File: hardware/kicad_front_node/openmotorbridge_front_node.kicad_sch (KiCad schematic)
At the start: 0 parts

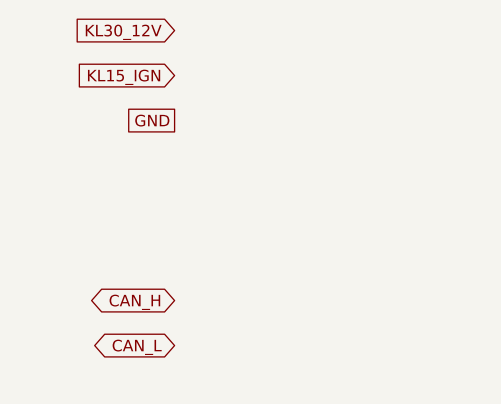
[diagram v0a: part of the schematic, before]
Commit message: feat(hardware): upgrade front node power architecture to dual power (pure USB bus-powered default + optional switched 12V KL15)
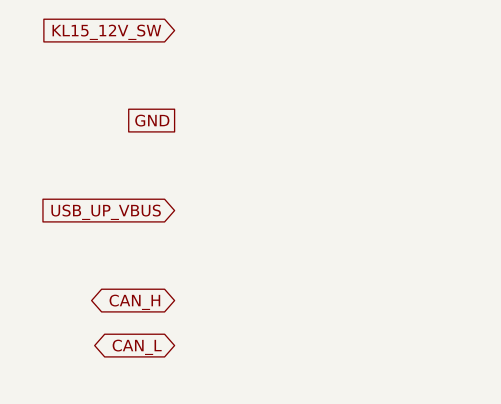
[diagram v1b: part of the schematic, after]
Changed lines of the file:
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@@
 		(title "OpenMotorBridge Universal Front Node (Cockpit & Smart Fairing)")
 		(date "2026-09-03")
-		(rev "v1.0")
+		(rev "v1.1")
 		(company "OpenMotorBridge Open Source Hardware")
-		(comment 1 "Automotive USB 2.0 Hub + CarPlay Power Switch + I2S Ambient Mic + CAN + Handlebar PTT + ESP-NOW")
+		(comment 1 "Dual Power: Pure USB Bus-Powered Standard + Optional Switched 12V (KL15 ACC)")
 	)
-	(global_label "KL30_12V" (shape input) (at 30.0 40.0 180) (effects (font (size 1.27 1.27)) (justify right)))
-	(global_label "KL15_IGN" (shape input) (at 30.0 45.0 180) (effects (font (size 1.27 1.27)) (justify right)))
+	(global_label "KL15_12V_SW" (shape input) (at 30.0 40.0 180) (effects (font (size 1.27 1.27)) (justify right)))
 	(global_label "GND" (shape passive) (at 30.0 50.0 180) (effects (font (size 1.27 1.27)) (justify right)))
+	(global_label "USB_UP_VBUS" (shape input) (at 30.0 60.0 180) (effects (font (size 1.27 1.27)) (justify right)))
 	(global_label "VCC_5V" (shape output) (at 80.0 40.0 0) (effects (font (size 1.27 1.27)) (justify left)))
 	(global_label "VCC_3V3" (shape output) (at 80.0 45.0 0) (effects (font (size 1.27 1.27)) (justify left)))

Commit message: docs & feat: restructure Chapter 08 reference kits, update modular enclosures, front-node mechanics and firmware
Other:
- title: OpenMotorBridge Universal Front Node (Cockpit & Smart Fairing) -> OpenMotorBridge Universal Front Node (Cockpit & Sensor Hub)
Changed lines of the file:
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@@
 	(paper "A3")
 	(title_block
-		(title "OpenMotorBridge Universal Front Node (Cockpit & Smart Fairing)")
+		(title "OpenMotorBridge Universal Front Node (Cockpit & Sensor Hub)")
 		(date "2026-09-03")
 		(rev "v1.1")

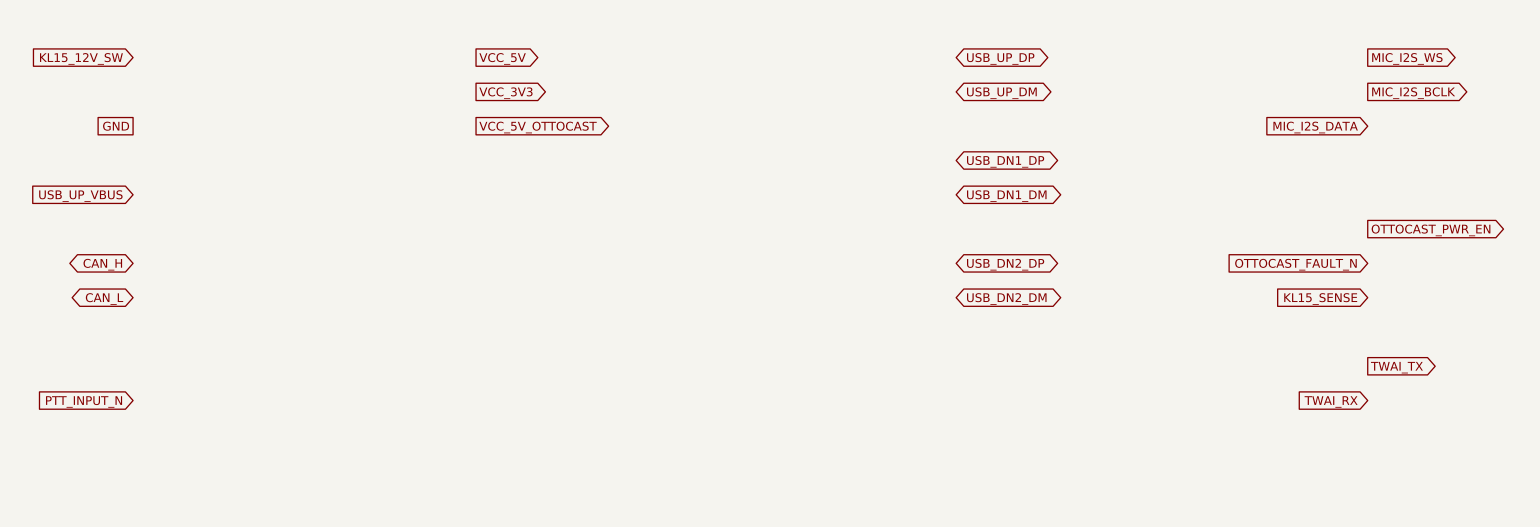
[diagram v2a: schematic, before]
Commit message: feat(hw,fw,pwa): implement PCBA 05 Front Node, LoRa alarm pager, universal TPMS, ESS strobe, privacy mute, and video telemetry export
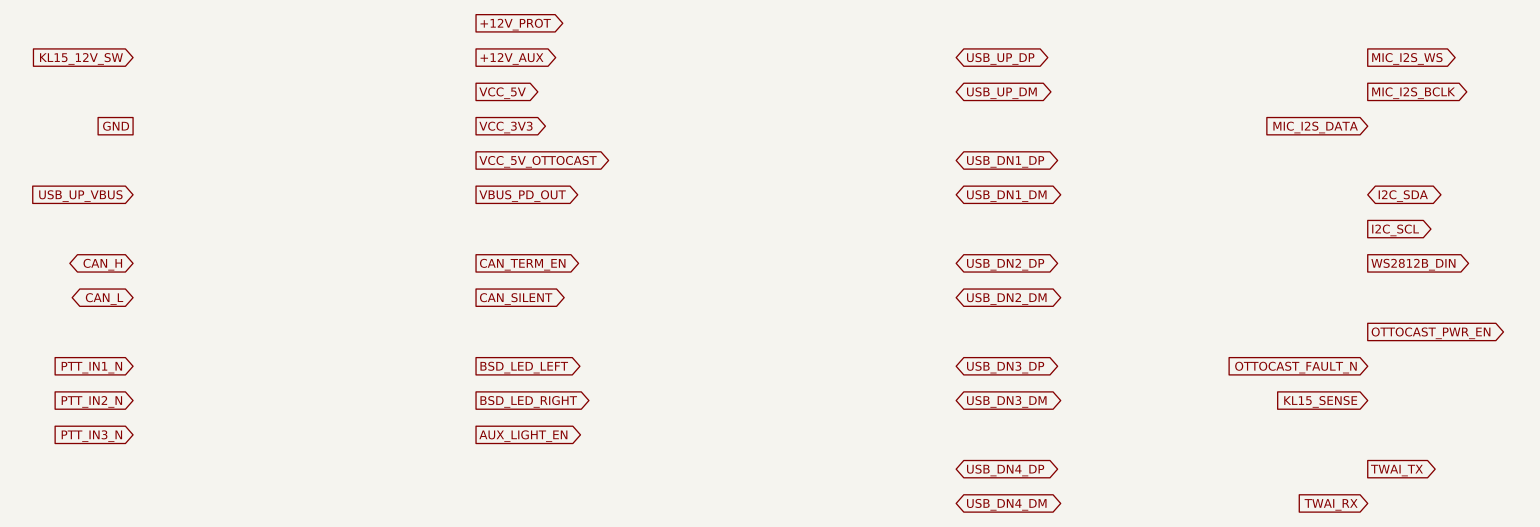
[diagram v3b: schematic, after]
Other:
- title: OpenMotorBridge Universal Front Node (Cockpit & Sensor Hub) -> OpenMotorBridge Universal Front Node (Cockpit & Sensor Hub PCBA 05)
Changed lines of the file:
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@@
 	(paper "A3")
 	(title_block
-		(title "OpenMotorBridge Universal Front Node (Cockpit & Sensor Hub)")
-		(date "2026-09-03")
-		(rev "v1.1")
+		(title "OpenMotorBridge Universal Front Node (Cockpit & Sensor Hub PCBA 05)")
+		(date "2026-09-12")
+		(rev "v2.0")
 		(company "OpenMotorBridge Open Source Hardware")
-		(comment 1 "Dual Power: Pure USB Bus-Powered Standard + Optional Switched 12V (KL15 ACC)")
+		(comment 1 "ESP32-S3, USB2514B 4-Port Hub, SC8102 USB-PD 20W, Qi 12V, Aux Light, BSD LEDs")
 	)
 	(global_label "KL15_12V_SW" (shape input) (at 30.0 40.0 180) (effects (font (size 1.27 1.27)) (justify right)))
+	(global_label "+12V_PROT" (shape output) (at 80.0 35.0 0) (effects (font (size 1.27 1.27)) (justify left)))
+	(global_label "+12V_AUX" (shape output) (at 80.0 40.0 0) (effects (font (size 1.27 1.27)) (justify left)))
 	(global_label "GND" (shape passive) (at 30.0 50.0 180) (effects (font (size 1.27 1.27)) (justify right)))
 	(global_label "USB_UP_VBUS" (shape input) (at 30.0 60.0 180) (effects (font (size 1.27 1.27)) (justify right)))
-	(global_label "VCC_5V" (shape output) (at 80.0 40.0 0) (effects (font (size 1.27 1.27)) (justify left)))
-	(global_label "VCC_3V3" (shape output) (at 80.0 45.0 0) (effects (font (size 1.27 1.27)) (justify left)))
-	(global_label "VCC_5V_OTTOCAST" (shape output) (at 80.0 50.0 0) (effects (font (size 1.27 1.27)) (justify left)))
+	(global_label "VCC_5V" (shape output) (at 80.0 45.0 0) (effects (font (size 1.27 1.27)) (justify left)))
+	(global_label "VCC_3V3" (shape output) (at 80.0 50.0 0) (effects (font (size 1.27 1.27)) (justify left)))
+	(global_label "VCC_5V_OTTOCAST" (shape output) (at 80.0 55.0 0) (effects (font (size 1.27 1.27)) (justify left)))
+	(global_label "VBUS_PD_OUT" (shape output) (at 80.0 60.0 0) (effects (font (size 1.27 1.27)) (justify left)))
 	(global_label "CAN_H" (shape bidirectional) (at 30.0 70.0 180) (effects (font (size 1.27 1.27)) (justify right)))
 	(global_label "CAN_L" (shape bidirectional) (at 30.0 75.0 180) (effects (font (size 1.27 1.27)) (justify right)))
-	(global_label "PTT_INPUT_N" (shape input) (at 30.0 90.0 180) (effects (font (size 1.27 1.27)) (justify right)))
+	(global_label "CAN_TERM_EN" (shape output) (at 80.0 70.0 0) (effects (font (size 1.27 1.27)) (justify left)))
+	(global_label "CAN_SILENT" (shape output) (at 80.0 75.0 0) (effects (font (size 1.27 1.27)) (justify left)))
+	(global_label "PTT_IN1_N" (shape input) (at 30.0 85.0 180) (effects (font (size 1.27 1.27)) (justify right)))
+	(global_label "PTT_IN2_N" (shape input) (at 30.0 90.0 180) (effects (font (size 1.27 1.27)) (justify right)))
+	(global_label "PTT_IN3_N" (shape input) (at 30.0 95.0 180) (effects (font (size 1.27 1.27)) (justify right)))
+	(global_label "BSD_LED_LEFT" (shape output) (at 80.0 85.0 0) (effects (font (size 1.27 1.27)) (justify left)))
+	(global_label "BSD_LED_RIGHT" (shape output) (at 80.0 90.0 0) (effects (font (size 1.27 1.27)) (justify left)))
+	(global_label "AUX_LIGHT_EN" (shape output) (at 80.0 95.0 0) (effects (font (size 1.27 1.27)) (justify left)))
 	(global_label "USB_UP_DP" (shape bidirectional) (at 150.0 40.0 0) (effects (font (size 1.27 1.27)) (justify left)))
 	(global_label "USB_UP_DM" (shape bidirectional) (at 150.0 45.0 0) (effects (font (size 1.27 1.27)) (justify left)))
@@
 	(global_label "USB_DN2_DP" (shape bidirectional) (at 150.0 70.0 0) (effects (font (size 1.27 1.27)) (justify left)))
 	(global_label "USB_DN2_DM" (shape bidirectional) (at 150.0 75.0 0) (effects (font (size 1.27 1.27)) (justify left)))
+	(global_label "USB_DN3_DP" (shape bidirectional) (at 150.0 85.0 0) (effects (font (size 1.27 1.27)) (justify left)))
+	(global_label "USB_DN3_DM" (shape bidirectional) (at 150.0 90.0 0) (effects (font (size 1.27 1.27)) (justify left)))
+	(global_label "USB_DN4_DP" (shape bidirectional) (at 150.0 100.0 0) (effects (font (size 1.27 1.27)) (justify left)))
+	(global_label "USB_DN4_DM" (shape bidirectional) (at 150.0 105.0 0) (effects (font (size 1.27 1.27)) (justify left)))
 	(global_label "MIC_I2S_WS" (shape output) (at 210.0 40.0 0) (effects (font (size 1.27 1.27)) (justify left)))
 	(global_label "MIC_I2S_BCLK" (shape output) (at 210.0 45.0 0) (effects (font (size 1.27 1.27)) (justify left)))
 	(global_label "MIC_I2S_DATA" (shape input) (at 210.0 50.0 180) (effects (font (size 1.27 1.27)) (justify right)))
-	(global_label "OTTOCAST_PWR_EN" (shape output) (at 210.0 65.0 0) (effects (font (size 1.27 1.27)) (justify left)))
-	(global_label "OTTOCAST_FAULT_N" (shape input) (at 210.0 70.0 180) (effects (font (size 1.27 1.27)) (justify right)))
-	(global_label "KL15_SENSE" (shape input) (at 210.0 75.0 180) (effects (font (size 1.27 1.27)) (justify right)))
-	(global_label "TWAI_TX" (shape output) (at 210.0 85.0 0) (effects (font (size 1.27 1.27)) (justify left)))
-	(global_label "TWAI_RX" (shape input) (at 210.0 90.0 180) (effects (font (size 1.27 1.27)) (justify right)))
+	(global_label "I2C_SDA" (shape bidirectional) (at 210.0 60.0 0) (effects (font (size 1.27 1.27)) (justify left)))
+	(global_label "I2C_SCL" (shape output) (at 210.0 65.0 0) (effects (font (size 1.27 1.27)) (justify left)))
+	(global_label "WS2812B_DIN" (shape output) (at 210.0 70.0 0) (effects (font (size 1.27 1.27)) (justify left)))
+	(global_label "OTTOCAST_PWR_EN" (shape output) (at 210.0 80.0 0) (effects (font (size 1.27 1.27)) (justify left)))
+	(global_label "OTTOCAST_FAULT_N" (shape input) (at 210.0 85.0 180) (effects (font (size 1.27 1.27)) (justify right)))
+	(global_label "KL15_SENSE" (shape input) (at 210.0 90.0 180) (effects (font (size 1.27 1.27)) (justify right)))
+	(global_label "TWAI_TX" (shape output) (at 210.0 100.0 0) (effects (font (size 1.27 1.27)) (justify left)))
+	(global_label "TWAI_RX" (shape input) (at 210.0 105.0 180) (effects (font (size 1.27 1.27)) (justify right)))
 )

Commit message: feat(hardware): implement dual independent 20W USB-PD subsystem for Lenker and Handschuhfach on PCBA 05
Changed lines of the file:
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@@
 	(title_block
 		(title "OpenMotorBridge Universal Front Node (Cockpit & Sensor Hub PCBA 05)")
-		(date "2026-09-12")
-		(rev "v2.0")
+		(date "2026-09-13")
+		(rev "v2.1")
 		(company "OpenMotorBridge Open Source Hardware")
-		(comment 1 "ESP32-S3, USB2514B 4-Port Hub, SC8102 USB-PD 20W, Qi 12V, Aux Light, BSD LEDs")
+		(comment 1 "ESP32-S3, USB2514B Hub, Dual SW3526 USB-PD 20W, Qi 12V, Aux Light, BSD LEDs")
 	)
 	(global_label "KL15_12V_SW" (shape input) (at 30.0 40.0 180) (effects (font (size 1.27 1.27)) (justify right)))
@@
 	(global_label "VCC_3V3" (shape output) (at 80.0 50.0 0) (effects (font (size 1.27 1.27)) (justify left)))
 	(global_label "VCC_5V_OTTOCAST" (shape output) (at 80.0 55.0 0) (effects (font (size 1.27 1.27)) (justify left)))
-	(global_label "VBUS_PD_OUT" (shape output) (at 80.0 60.0 0) (effects (font (size 1.27 1.27)) (justify left)))
+	(global_label "VBUS_PD1_OUT" (shape output) (at 80.0 60.0 0) (effects (font (size 1.27 1.27)) (justify left)))
+	(global_label "VBUS_PD3_OUT" (shape output) (at 80.0 65.0 0) (effects (font (size 1.27 1.27)) (justify left)))
 	(global_label "CAN_H" (shape bidirectional) (at 30.0 70.0 180) (effects (font (size 1.27 1.27)) (justify right)))
 	(global_label "CAN_L" (shape bidirectional) (at 30.0 75.0 180) (effects (font (size 1.27 1.27)) (justify right)))
@@
 	(global_label "BSD_LED_RIGHT" (shape output) (at 80.0 90.0 0) (effects (font (size 1.27 1.27)) (justify left)))
 	(global_label "AUX_LIGHT_EN" (shape output) (at 80.0 95.0 0) (effects (font (size 1.27 1.27)) (justify left)))
+	(global_label "USB_DN1_CC" (shape bidirectional) (at 80.0 100.0 0) (effects (font (size 1.27 1.27)) (justify left)))
+	(global_label "USB_DN3_CC" (shape bidirectional) (at 80.0 105.0 0) (effects (font (size 1.27 1.27)) (justify left)))
 	(global_label "USB_UP_DP" (shape bidirectional) (at 150.0 40.0 0) (effects (font (size 1.27 1.27)) (justify left)))
 	(global_label "USB_UP_DM" (shape bidirectional) (at 150.0 45.0 0) (effects (font (size 1.27 1.27)) (justify left)))

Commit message: feat(hw): finalize PCB lineup routing, sync PCBA 03 cartridge with J_PROG header and DTM12 schematics
- PCBA 01 (Central Box): Remediate net routing, DTM12 hierarchical schematic synchronization, 100% routed, 0 DRC errors.
- PCBA 03 (Smart Modular Cartridge): Position and route J_PROG 4-pin SMD programming header on F.Cu at (108.0, 89.61), synchronize CPL and schematic, 100% routed, 0 DRC errors.
- PCBA 05 (Universal Front Node): Preconnect and routing verified, 100% routed, 0 DRC errors.
- PCBA 07 (LoRa Smart-Keyfob): Routing and DRC verified, 100% routed, 0 DRC errors.
- PCBA 08 (Radar 2.0 Sub-MCU & Wings): Sub-MCU routing and HF isolation verified, 100% routed, 0 DRC errors.
- PCBA 10 (OMM 446 PMR/DMR Intercom): KiCad DRC verified, 100% routed, 0 DRC errors.
- Firmware: Align configuration headers across front_node and smart_cartridge.
- Tools: Add comprehensive preflight PCBA audit suite tools/audit_pcbas_preflight.py.
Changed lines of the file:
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@@
 	(global_label "TWAI_TX" (shape output) (at 210.0 100.0 0) (effects (font (size 1.27 1.27)) (justify left)))
 	(global_label "TWAI_RX" (shape input) (at 210.0 105.0 180) (effects (font (size 1.27 1.27)) (justify right)))
+	(global_label "UWB_SCK" (shape output) (at 210.0 115.0 0) (effects (font (size 1.27 1.27)) (justify left)))
+	(global_label "UWB_MOSI" (shape output) (at 210.0 120.0 0) (effects (font (size 1.27 1.27)) (justify left)))
+	(global_label "UWB_MISO" (shape input) (at 210.0 125.0 180) (effects (font (size 1.27 1.27)) (justify right)))
+	(global_label "UWB_CS" (shape output) (at 210.0 130.0 0) (effects (font (size 1.27 1.27)) (justify left)))
+	(global_label "UWB_IRQ" (shape input) (at 210.0 135.0 180) (effects (font (size 1.27 1.27)) (justify right)))
+	(global_label "UWB_RST" (shape output) (at 210.0 140.0 0) (effects (font (size 1.27 1.27)) (justify left)))
+	(global_label "UWB_RF" (shape passive) (at 210.0 145.0 0) (effects (font (size 1.27 1.27)) (justify left)))
 )

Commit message: fix(frontnode): synchronize PCBA 05 schematic with PCB and pass prefab-gate check
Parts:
- added ANT_UWB: Taoglas_FXUWB10, Connector_Coaxial:U.FL_Hirose_U.FL-R-SMT-1_Vertical, symbol ANT_UWB_sym
- added C19: 10uF_50V, C_0805_2012Metric, symbol C19_sym
- added C22: 22uF_16V, C_0805_2012Metric, symbol C22_sym
- added C24: 2.2uF_3V3, C_0603_1608Metric, symbol C24_sym
- added C25: 10uF_50V_PD1, C_0805_2012Metric, symbol C25_sym
- added C26: 22uF_25V_PD1, C_0805_2012Metric, symbol C26_sym
- added C27: 10uF_50V_PD3, C_0805_2012Metric, symbol C27_sym
- added C28: 22uF_25V_PD3, C_0805_2012Metric, symbol C28_sym
- added C_BUF: 470uF_10V_POLYMER, CP_EIA-7343-31_Kemet-D, symbol C_BUF_sym
- added D4: SMCJ36CA_TVS, D_SMB, symbol D4_sym
- added D5: SS34_REV_POL, D_SMA, symbol D5_sym
- added D7: SS34_USB_OR, D_SMA, symbol D7_sym
- added D8: SS34_BUCK_OR, D_SMA, symbol D8_sym
- added H1: M2.5_MOUNT, MountingHole_2.7mm_M2.5_Pad_Via, symbol H1_sym
- added H2: M2.5_MOUNT, MountingHole_2.7mm_M2.5_Pad_Via, symbol H2_sym
- added H3: M2.5_MOUNT, MountingHole_2.7mm_M2.5_Pad_Via, symbol H3_sym
- added H4: M2.5_MOUNT, MountingHole_2.7mm_M2.5_Pad_Via, symbol H4_sym
- added J1: 12V_KL15_GND, JST_PH_B2B-PH-K_1x02_P2.00mm_Vertical, symbol J1_sym
- added J10: 12V_QI_POWER, JST_PH_B2B-PH-K_1x02_P2.00mm_Vertical, symbol J10_sym
- added J11: 12V_AUX_LIGHT, JST_PH_B2B-PH-K_1x02_P2.00mm_Vertical, symbol J11_sym
- added J12: QWIIC_I2C, JST_SH_BM04B-SRSS-TB_1x04-1MP_P1.00mm_Vertical, symbol J12_sym
- added J2: CAN_H_L_GND, JST_PH_B3B-PH-K_1x03_P2.00mm_Vertical, symbol J2_sym
- added J3: HANDLEBAR_MULTI_BTN, JST_PH_B4B-PH-K_1x04_P2.00mm_Vertical, symbol J3_sym
- added J4: USB_UPSTREAM_HOST, JST_PH_B4B-PH-K_1x04_P2.00mm_Vertical, symbol J4_sym
- added J5: USB_DN1_PHONE_PD20W, JST_PH_B5B-PH-K_1x05_P2.00mm_Vertical, symbol J5_sym
- added J5_MP3: USB_DN3_GLOVEBOX_PD20W, JST_PH_B5B-PH-K_1x05_P2.00mm_Vertical, symbol J5_MP3_sym
- added J6: USB_DN2_CP2AA_PIGTAIL, JST_PH_B4B-PH-K_1x04_P2.00mm_Vertical, symbol J6_sym
- added J6_AUX: USB_DN4_COCKPIT_AUX, JST_PH_B4B-PH-K_1x04_P2.00mm_Vertical, symbol J6_AUX_sym
- added J7: USB-C_SERVICE, USB_C_Receptacle_HRO_TYPE-C-31-M-12, symbol J7_sym
- added J8: ACTION_CAM_5V_PWR, JST_PH_B2B-PH-K_1x02_P2.00mm_Vertical, symbol J8_sym
- added J9: MIRROR_BSD_LEDS, JST_PH_B3B-PH-K_1x03_P2.00mm_Vertical, symbol J9_sym
- added K1: CPC1017N_CAN_RELAY, SOP-4_4.4x2.6mm_P1.27mm, symbol K1_sym
- added L1: 4.7uH_Power_Choke, L_Sunlord_MWSA1206S-470, symbol L1_sym
- added L2: 4.7uH_PD1_Choke, L_Sunlord_MWSA0503S, symbol L2_sym
- added L3: 4.7uH_PD3_Choke, L_Sunlord_MWSA0503S, symbol L3_sym
- added LED1: WS2812B-2020_RGB, LED_WS2812B-2020_PLCC4_2.0x2.0mm, symbol LED1_sym
- added MIC1: MSM261S4030H0R, InvenSense_ICS-43434-6_3.5x2.65mm, symbol MIC1_sym
- added MK1: SPH0645LM4H, Sensor_Audio:Knowles_SPH0645LM4H, symbol MK1_sym
- added Q1: DMN63D8_BSD_MOSFET, SOT-363_SC-70-6, symbol Q1_sym
- added Q2: TPS1H100_AUX_LIGHT, Texas_HTSSOP-14-1EP_4.4x5mm_P0.65mm_EP3.4x5mm_Mask3.155x3.255mm_ThermalVias, symbol Q2_sym
- added R10: 120R_CAN, R_0603_1608Metric, symbol R10_sym
- added R15: 5.1k_CC1, R_0603_1608Metric, symbol R15_sym
- added R16: 5.1k_CC2, R_0603_1608Metric, symbol R16_sym
- added R5: 12k_RBIAS, R_0603_1608Metric, symbol R5_sym
- added R8: 10k_FAULT, R_0603_1608Metric, symbol R8_sym
- added SW1: BOOT, SW_Push_SPST_NO_Alps_SKRK, symbol SW1_sym
- added SW2: RESET, SW_Push_SPST_NO_Alps_SKRK, symbol SW2_sym
- added U1: ESP32-S3-WROOM-1U, ESP32-S3-WROOM-1U, symbol U1_sym
- added U2: USB2514Bi-AEZG, QFN-36-1EP_6x6mm_P0.5mm_EP4.1x4.1mm, symbol U2_sym
- added U3: TPS54302_5V_BUCK, SOT-23-6, symbol U3_sym
- added U4: TPS2051B_PORT2_GATE, SOT-23-5, symbol U4_sym
- added U5: SW3526_USB_PD1_20W, QFN-28-1EP_4x4mm_P0.4mm_EP2.4x2.4mm_ThermalVias, symbol U5_sym
- added U6: TCAN334G_CAN, SOIC-8_3.9x4.9mm_P1.27mm, symbol U6_sym
- added U7: TLV75533P_3V3_LDO, SOT-23-5, symbol U7_sym
- added U8: SW3526_USB_PD3_20W, QFN-28-1EP_4x4mm_P0.4mm_EP2.4x2.4mm_ThermalVias, symbol U8_sym
- added U9: DW3110, Package_DFN_QFN:QFN-16-1EP_3x3mm_P0.5mm_EP1.7x1.7mm_ThermalVias, symbol U9_sym
- added Y1: 24.000MHz, Crystal_SMD_3225-4Pin_3.2x2.5mm, symbol Y1_sym
- added Y_UWB: 38.4MHz, Crystal:Crystal_SMD_2016-4Pin_2.0x1.6mm, symbol Y_UWB_sym
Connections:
- net +12V_AUX: now also J11.1 (+12V_AUX), Q2.6 (+12V_AUX), Q2.7 (+12V_AUX), Q2.8 (+12V_AUX)
- net +12V_PROT: now also C19.1 (+12V_PROT), C25.1 (+12V_PROT), C27.1 (+12V_PROT), D4.1 (+12V_PROT), D5.2 (+12V_PROT), J10.1 (+12V_PROT), J9.1 (+12V_PROT), Q2.11 (+12V_PROT), Q2.12 (+12V_PROT), Q2.13 (+12V_PROT), Q2.14 (+12V_PROT), Q2.15 (+12V_PROT), U3.3 (+12V_PROT), U3.5 (+12V_PROT), U5.1 (+12V_PROT), U5.2 (+12V_PROT), U5.28 (+12V_PROT), U8.1 (+12V_PROT), U8.2 (+12V_PROT), U8.28 (+12V_PROT)
- net AUX_LIGHT_EN: now also Q2.2 (AUX_LIGHT_EN), U1.22 (AUX_LIGHT_EN)
- net BSD_LED_LEFT: now also Q1.2 (BSD_LED_LEFT), U1.20 (BSD_LED_LEFT)
- net BSD_LED_RIGHT: now also Q1.5 (BSD_LED_RIGHT), U1.21 (BSD_LED_RIGHT)
- net CAN_H: now also J2.1 (CAN_H), K1.3 (CAN_H), U6.7 (CAN_H)
- net CAN_L: now also J2.2 (CAN_L), R10.2 (CAN_L), U6.6 (CAN_L)
- net CAN_SILENT: now also U1.5 (CAN_SILENT), U6.8 (CAN_SILENT)
- net CAN_TERM_EN: now also K1.1 (CAN_TERM_EN), U1.15 (CAN_TERM_EN)
- net GND: now also ANT_UWB.2 (GND), C19.2 (GND), C22.2 (GND), C24.2 (GND), C25.2 (GND), C26.2 (GND), C27.2 (GND), C28.2 (GND), C_BUF.2 (GND), D4.2 (GND), H1.1 (GND), H2.1 (GND), H3.1 (GND), H4.1 (GND), J1.2 (GND), J10.2 (GND), J11.2 (GND), J12.1 (GND), J12.MP (GND), J2.3 (GND), J3.1 (GND), J4.4 (GND), J5.5 (GND), J5_MP3.5 (GND), J6.4 (GND), J6_AUX.4 (GND), J7.A1 (GND), J7.A12 (GND), J7.B1 (GND), J7.B12 (GND), J7.SH (GND), J8.2 (GND), K1.2 (GND), LED1.2 (GND), LED1.3 (GND), MIC1.2 (GND), MIC1.3 (GND), MK1.5 (GND), Q1.1 (GND), Q1.4 (GND), Q2.1 (GND), Q2.4 (GND), R15.2 (GND), R16.2 (GND), R5.2 (GND), SW1.2 (GND), SW2.2 (GND), U1.1 (GND), U1.40 (GND), U1.41 (GND), U2.11 (GND), U2.25 (GND), U2.28 (GND), U2.34 (GND), U2.37 (GND), U3.1 (GND), U4.2 (GND), U5.14 (GND), U5.29 (GND), U6.2 (GND), U6.5 (GND), U7.2 (GND), U7.4 (GND), U8.14 (GND), U8.29 (GND), U9.1 (GND), U9.11 (GND), U9.16 (GND), U9.17 (GND), U9.2 (GND), U9.3 (GND), U9.6 (GND), Y1.2 (GND), Y1.4 (GND), Y_UWB.2 (GND), Y_UWB.4 (GND)
- net I2C_SCL: now also J12.4 (I2C_SCL), U1.18 (I2C_SCL)
- net I2C_SDA: now also J12.3 (I2C_SDA), U1.17 (I2C_SDA)
- net KL15_12V_SW: now also D5.1 (KL15_12V_SW), J1.1 (KL15_12V_SW)
- net MIC_I2S_BCLK: now also MIC1.4 (MIC_I2S_BCLK), MK1.2 (MIC_I2S_BCLK), U1.7 (MIC_I2S_BCLK)
- net MIC_I2S_DATA: now also MIC1.6 (MIC_I2S_DATA), MK1.1 (MIC_I2S_DATA), U1.12 (MIC_I2S_DATA)
- net MIC_I2S_WS: now also MIC1.1 (MIC_I2S_WS), MK1.3 (MIC_I2S_WS), U1.6 (MIC_I2S_WS)
- net OTTOCAST_FAULT_N: now also R8.2 (OTTOCAST_FAULT_N), U1.38 (OTTOCAST_FAULT_N), U2.17 (OTTOCAST_FAULT_N), U4.3 (OTTOCAST_FAULT_N)
- net OTTOCAST_PWR_EN: now also U1.39 (OTTOCAST_PWR_EN), U4.4 (OTTOCAST_PWR_EN)
- net PTT_IN1_N: now also J3.2 (PTT_IN1_N), U1.8 (PTT_IN1_N)
- net PTT_IN2_N: now also J3.3 (PTT_IN2_N), U1.9 (PTT_IN2_N)
- net PTT_IN3_N: now also J3.4 (PTT_IN3_N), U1.10 (PTT_IN3_N)
- net TWAI_RX: now also U1.36 (TWAI_RX), U6.4 (TWAI_RX)
- net TWAI_TX: now also U1.23 (TWAI_TX), U6.1 (TWAI_TX)
- net USB_DN1_CC: now also J5.4 (USB_DN1_CC), U5.18 (USB_DN1_CC), U5.19 (USB_DN1_CC)
- net USB_DN1_DM: now also J5.2 (USB_DN1_DM), U2.1 (USB_DN1_DM), U5.17 (USB_DN1_DM)
- net USB_DN1_DP: now also J5.3 (USB_DN1_DP), U2.2 (USB_DN1_DP), U5.16 (USB_DN1_DP)
- net USB_DN2_DM: now also J6.2 (USB_DN2_DM), U2.3 (USB_DN2_DM)
- net USB_DN2_DP: now also J6.3 (USB_DN2_DP), U2.4 (USB_DN2_DP)
- net USB_DN3_CC: now also J5_MP3.4 (USB_DN3_CC), U8.18 (USB_DN3_CC), U8.19 (USB_DN3_CC)
- net USB_DN3_DM: now also J5_MP3.2 (USB_DN3_DM), U2.6 (USB_DN3_DM), U8.17 (USB_DN3_DM)
- net USB_DN3_DP: now also J5_MP3.3 (USB_DN3_DP), U2.7 (USB_DN3_DP), U8.16 (USB_DN3_DP)
- net USB_DN4_DM: now also J6_AUX.2 (USB_DN4_DM), U2.8 (USB_DN4_DM)
- net USB_DN4_DP: now also J6_AUX.3 (USB_DN4_DP), U2.9 (USB_DN4_DP)
- net USB_UP_DM: now also J4.2 (USB_UP_DM), U2.30 (USB_UP_DM)
- net USB_UP_DP: now also J4.3 (USB_UP_DP), U2.31 (USB_UP_DP)
- net USB_UP_VBUS: now also D7.2 (USB_UP_VBUS), J4.1 (USB_UP_VBUS)
- net UWB_CS: now also U1.33 (UWB_CS), U9.10 (UWB_CS)
- net UWB_IRQ: now also U1.34 (UWB_IRQ), U9.13 (UWB_IRQ)
- net UWB_MISO: now also U1.32 (UWB_MISO), U9.8 (UWB_MISO)
- net UWB_MOSI: now also U1.31 (UWB_MOSI), U9.9 (UWB_MOSI)
- net UWB_RF: now also ANT_UWB.1 (UWB_RF), U9.15 (UWB_RF)
- net UWB_RST: now also U1.35 (UWB_RST), U9.12 (UWB_RST)
- net UWB_SCK: now also U1.30 (UWB_SCK), U9.7 (UWB_SCK)
- net VBUS_PD1_OUT: now also C26.1 (VBUS_PD1_OUT), J5.1 (VBUS_PD1_OUT), L2.2 (VBUS_PD1_OUT), U5.21 (VBUS_PD1_OUT)
- net VBUS_PD3_OUT: now also C28.1 (VBUS_PD3_OUT), J5_MP3.1 (VBUS_PD3_OUT), L3.2 (VBUS_PD3_OUT), U8.21 (VBUS_PD3_OUT)
- net VCC_3V3: now also C24.1 (VCC_3V3), J12.2 (VCC_3V3), MIC1.5 (VCC_3V3), MK1.4 (VCC_3V3), Q2.3 (VCC_3V3), R8.1 (VCC_3V3), U1.2 (VCC_3V3), U2.10 (VCC_3V3), U2.12 (VCC_3V3), U2.13 (VCC_3V3), U2.15 (VCC_3V3), U2.16 (VCC_3V3), U2.18 (VCC_3V3), U2.19 (VCC_3V3), U2.20 (VCC_3V3), U2.21 (VCC_3V3), U2.22 (VCC_3V3), U2.23 (VCC_3V3), U2.24 (VCC_3V3), U2.26 (VCC_3V3), U2.27 (VCC_3V3), U2.29 (VCC_3V3), U2.36 (VCC_3V3), U2.5 (VCC_3V3), U6.3 (VCC_3V3), U7.5 (VCC_3V3), U9.14 (VCC_3V3)
- net VCC_5V: now also C22.1 (VCC_5V), C_BUF.1 (VCC_5V), D7.1 (VCC_5V), D8.2 (VCC_5V), J6_AUX.1 (VCC_5V), J7.A4 (VCC_5V), J7.A9 (VCC_5V), J7.B4 (VCC_5V), J7.B9 (VCC_5V), J8.1 (VCC_5V), LED1.1 (VCC_5V), U4.5 (VCC_5V), U7.1 (VCC_5V), U7.3 (VCC_5V)
- net VCC_5V_OTTOCAST: now also J6.1 (VCC_5V_OTTOCAST), U4.1 (VCC_5V_OTTOCAST)
- net WS2812B_DIN: now also LED1.4 (WS2812B_DIN), U1.19 (WS2812B_DIN)
- new net BSD_LEFT_N: J9.2 (BSD_LEFT_N), Q1.6 (BSD_LEFT_N)
- new net BSD_RIGHT_N: J9.3 (BSD_RIGHT_N), Q1.3 (BSD_RIGHT_N)
- new net CAN_TERM_R: K1.4 (CAN_TERM_R), R10.1 (CAN_TERM_R)
- new net ESP_BOOT: SW1.1 (ESP_BOOT), U1.27 (ESP_BOOT)
- new net ESP_EN: SW2.1 (ESP_EN), U1.3 (ESP_EN)
- new net HUB_RBIAS: R5.1 (HUB_RBIAS), U2.35 (HUB_RBIAS)
- new net SW_BUCK: L1.1 (SW_BUCK), U3.2 (SW_BUCK)
- new net SW_PD1_BUCK: L2.1 (SW_PD1_BUCK), U5.25 (SW_PD1_BUCK), U5.26 (SW_PD1_BUCK), U5.27 (SW_PD1_BUCK)
- new net SW_PD3_BUCK: L3.1 (SW_PD3_BUCK), U8.25 (SW_PD3_BUCK), U8.26 (SW_PD3_BUCK), U8.27 (SW_PD3_BUCK)
- new net USB_CC1: J7.A5 (USB_CC1), R15.1 (USB_CC1)
- new net USB_CC2: J7.B5 (USB_CC2), R16.1 (USB_CC2)
- new net USB_SERV_DM: J7.A7 (USB_SERV_DM), J7.B7 (USB_SERV_DM), U1.13 (USB_SERV_DM)
- new net USB_SERV_DP: J7.A6 (USB_SERV_DP), J7.B6 (USB_SERV_DP), U1.14 (USB_SERV_DP)
- new net UWB_XTAL1: U9.4 (UWB_XTAL1), Y_UWB.1 (UWB_XTAL1)
- new net UWB_XTAL2: U9.5 (UWB_XTAL2), Y_UWB.3 (UWB_XTAL2)
- new net VBUS_BUCK_OUT: D8.1 (VBUS_BUCK_OUT), L1.2 (VBUS_BUCK_OUT)
- new net XTAL_IN: U2.33 (XTAL_IN), Y1.1 (XTAL_IN)
- new net XTAL_OUT: U2.32 (XTAL_OUT), Y1.3 (XTAL_OUT)
